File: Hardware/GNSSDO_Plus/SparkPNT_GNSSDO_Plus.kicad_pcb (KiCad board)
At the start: 4 copper layers, 151.9 x 101.6 mm, 472 parts, among them J1 SMA_Edge, J10 SMA_Edge, J2 USB_C_Receptacle, J3 SMA_Edge, J4 USB_C_Receptacle, J5 MagJack_PoE, J6 microSD, J7 Qwiic_Vertical, J8 SMA_Edge, J9 Screw_Cage_3.5mm-10, Q1 MBT3904DW1, Q2 DMG2305UX, Q3 DMG2305UX, Q4 DMG2305UX, Q5 DMG2305UX, Q6 DMG2305UX, Q7 DMG2305UX, Q8 DMG2305UX, Q9 DMG2305UX, SW1 PTH_RA_h7.5mm, SW2 PTH_RA_h7.5mm, SW3 PTH_RA_h7.5mm, SW4 DPDT_Slide_SMD_7.2x3.5mm, U1 ESP32-WROVER-IE-N16R8, U10 74LVC2T45DC, U11 AP7361C-3.3V, U12 74LVC2T45DC, U13 STP3593LF, U14 74LVC2T45DC, U15 SN74LVC1G175DCK, U16 JPS-3-1+, U17 LMV7219M5, U18 MS8607-02BA, U19 PCA9306, U2 mosaic-T, U20 LMV7219M5, U23 LMV7219M5, U24 LMV7219M5, U25 AP2112K-3.3, U26 LTC4418, U27 LTC4418, U3 CH340C, U4 KSZ8041NL/I, U5 AP7361C-3.3V, U6 REC15E-2405SZ, U7 DP5305, U8 74LVC2T45DC, U9 74LVC2T45DC

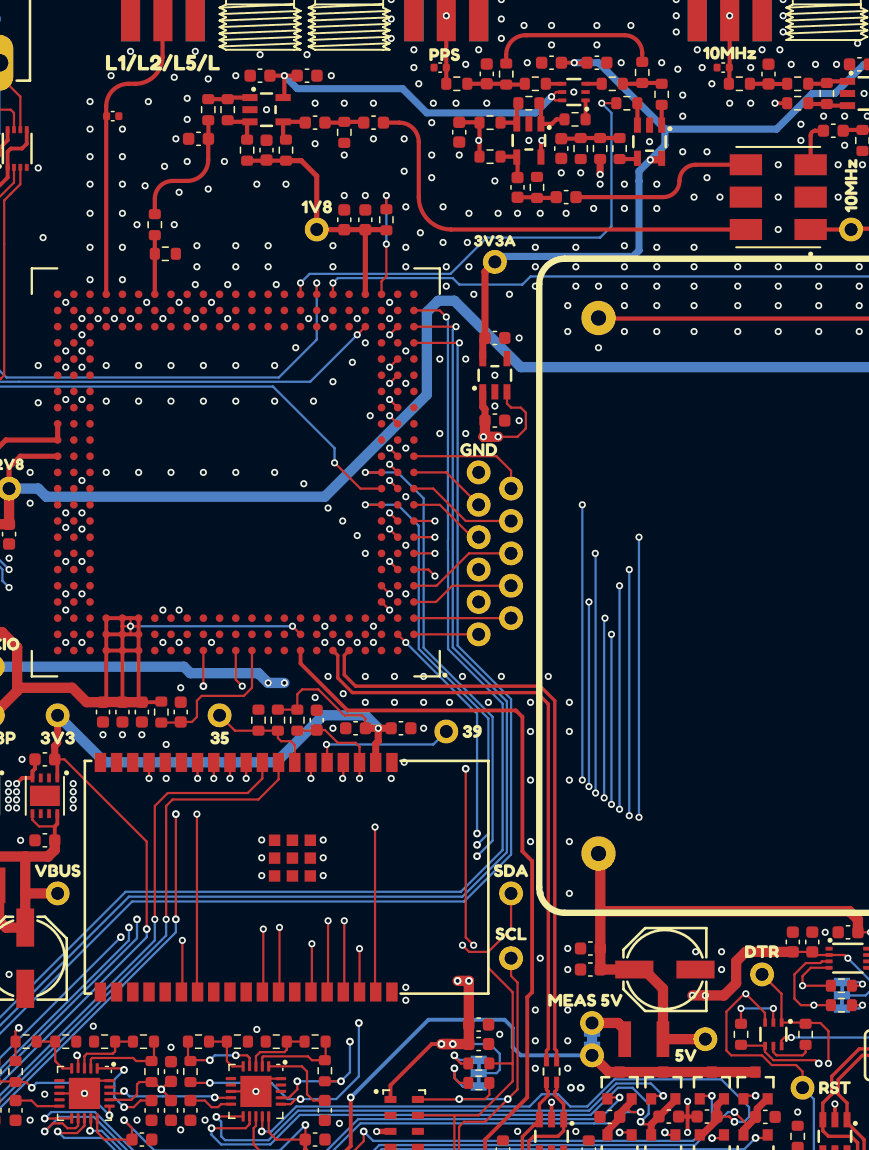
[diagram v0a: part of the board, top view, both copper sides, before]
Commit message: Update GNSSDO KiCad files to match latest SparkFun library
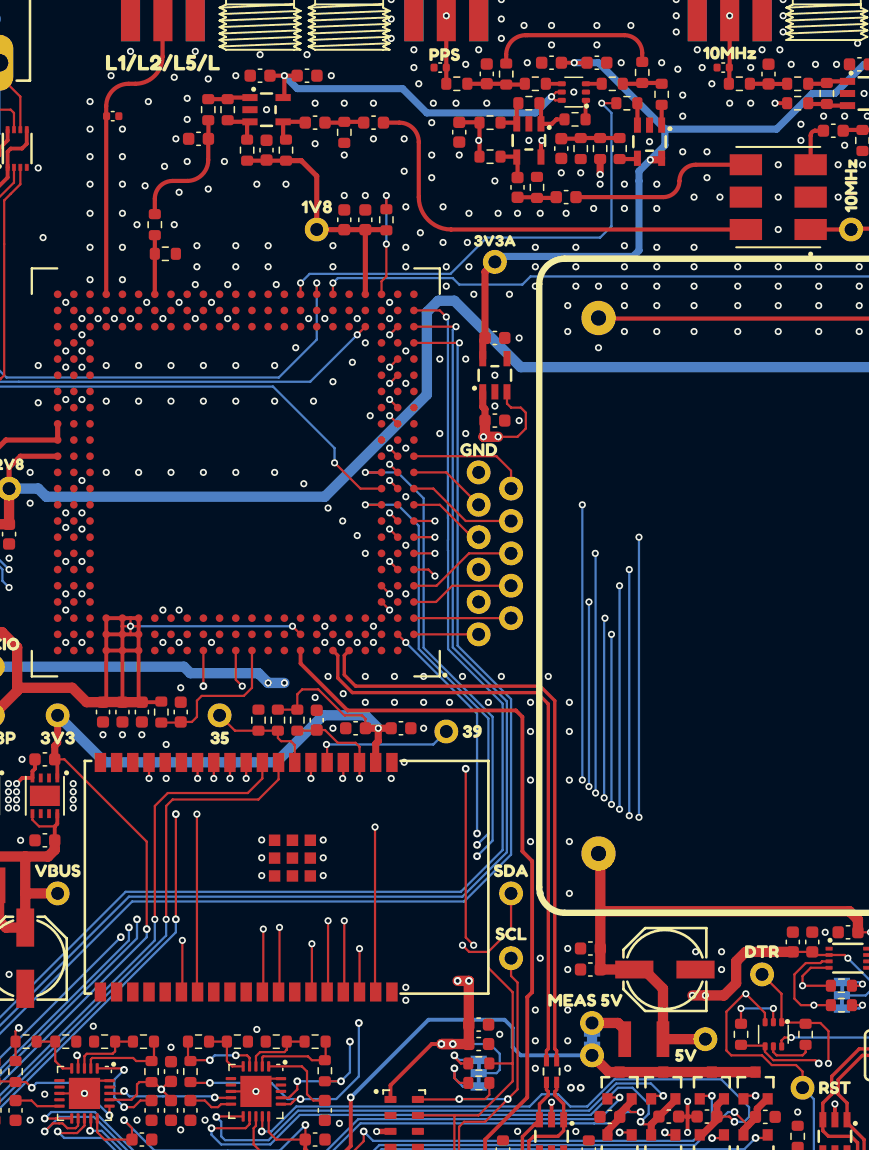
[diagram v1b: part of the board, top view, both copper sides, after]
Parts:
- C9: value 1nF -> 1.0nF
- J1, J10, J3, J8: footprint SparkFun-Connector:SMA_Edge -> SparkFun-Connector:SMA_Edge_6.3mm
- J7: footprint SparkFun-Connector:JST_SMD_1.0mm-4_Vertical_Black -> SparkFun-Connector:JST_1x04_P1.0mm_Vertical_SMD
- J9: footprint SparkFun-Connector:Screw_Cage_3.5mm-10 -> SparkFun-Connector:ScrewCage_1x10_P3.5mm_Horizontal
- L1, L2: value 470Ohm -> 470 Ohm
- Q1, U15: footprint SparkFun-Semiconductor-Standard:SOT-323 -> SparkFun-Semiconductor-Standard:SOT-363_SC-70-6
- TP1, TP10, TP11, TP12, TP13, TP14, TP15, TP16, TP17, TP18, TP19, TP2, TP21, TP22, TP23, TP24, TP25, TP26, TP27, TP28, TP29, TP3, TP33, TP34, TP35, TP36, TP37, TP38, TP39, TP4, TP40, TP41, TP43, TP5, TP6, TP7, TP8, TP9: footprint SparkFun-Connector:1x01 -> SparkFun-Connector:1x01_P2.54mm
- TR1: footprint SparkFun-Coil:RFCMF1220100M4T -> SparkFun-Coil:Choke_100MHz_USB
- U2: footprint SparkFun-GPS:MOSAIC_LGA -> SparkFun-GNSS:Septentrio_mosaic_LGA
